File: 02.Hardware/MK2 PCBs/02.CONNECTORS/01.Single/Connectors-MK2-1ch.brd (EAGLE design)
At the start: 59.5 x 28.5 mm, 3 parts, among them K1 FLEX8

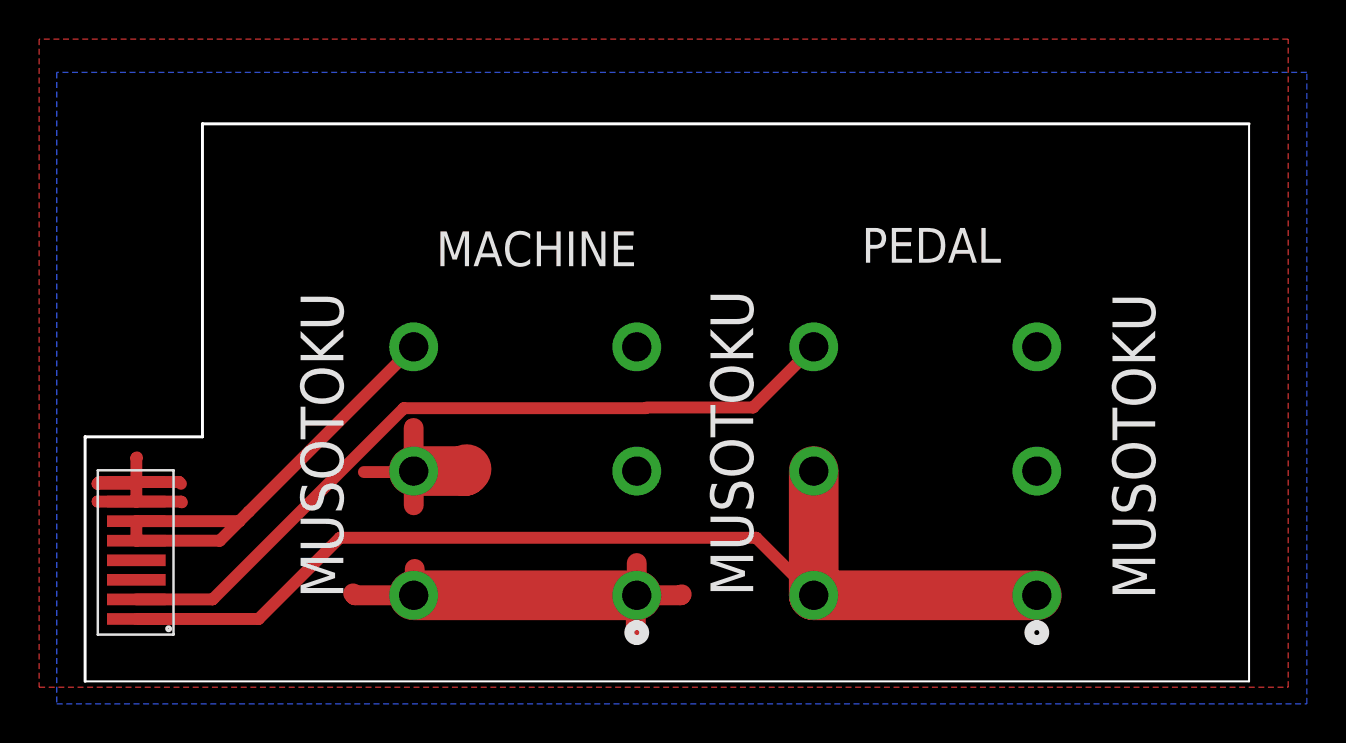
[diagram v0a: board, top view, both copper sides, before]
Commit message: Cambio Grosor y Carpetas nuevas
Se cambia el grosor de las pistas de VOUT y la conexión a las vías de los conectores.
----------
Creación de las carpetas dentro de la
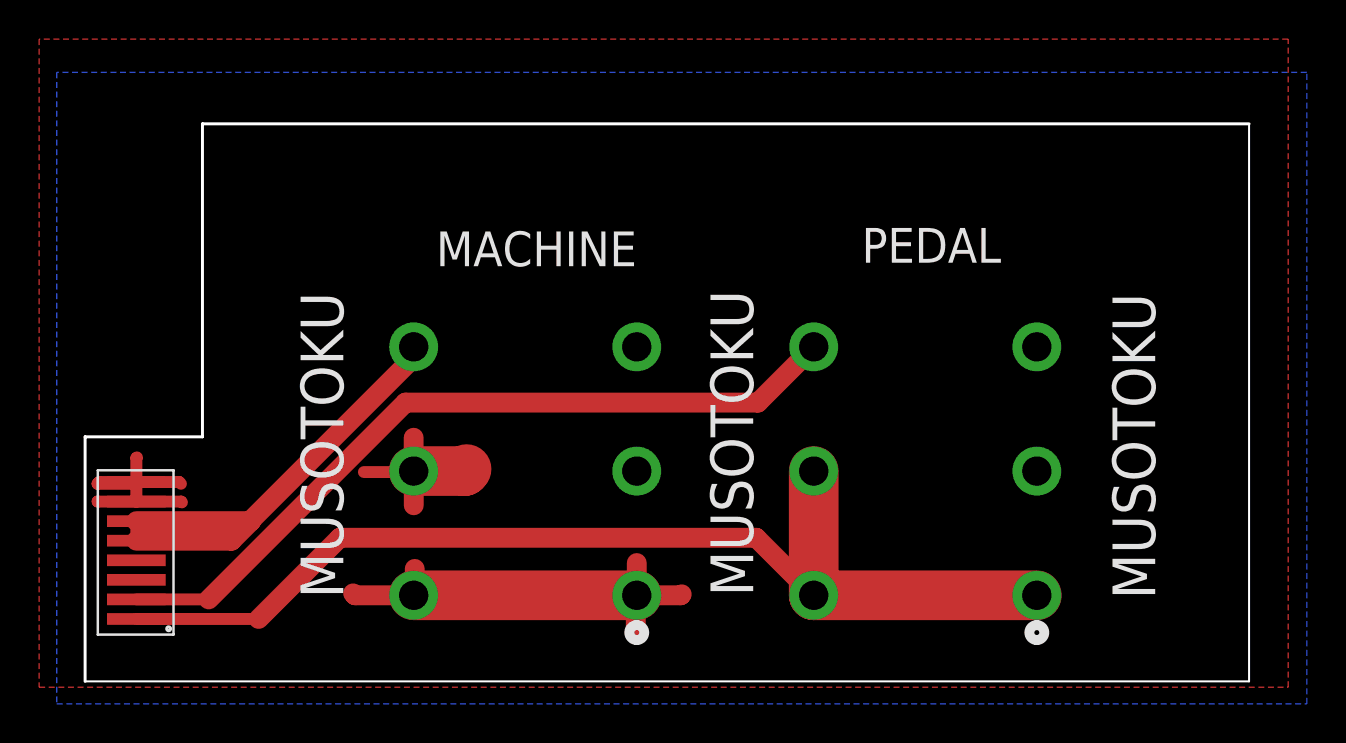
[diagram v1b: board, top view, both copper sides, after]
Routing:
- net VOUT: track 24.5 -> 25.5 mm
- net GND: track 50.9 -> 50.3 mm

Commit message: PCB 1channel - CAM output generado
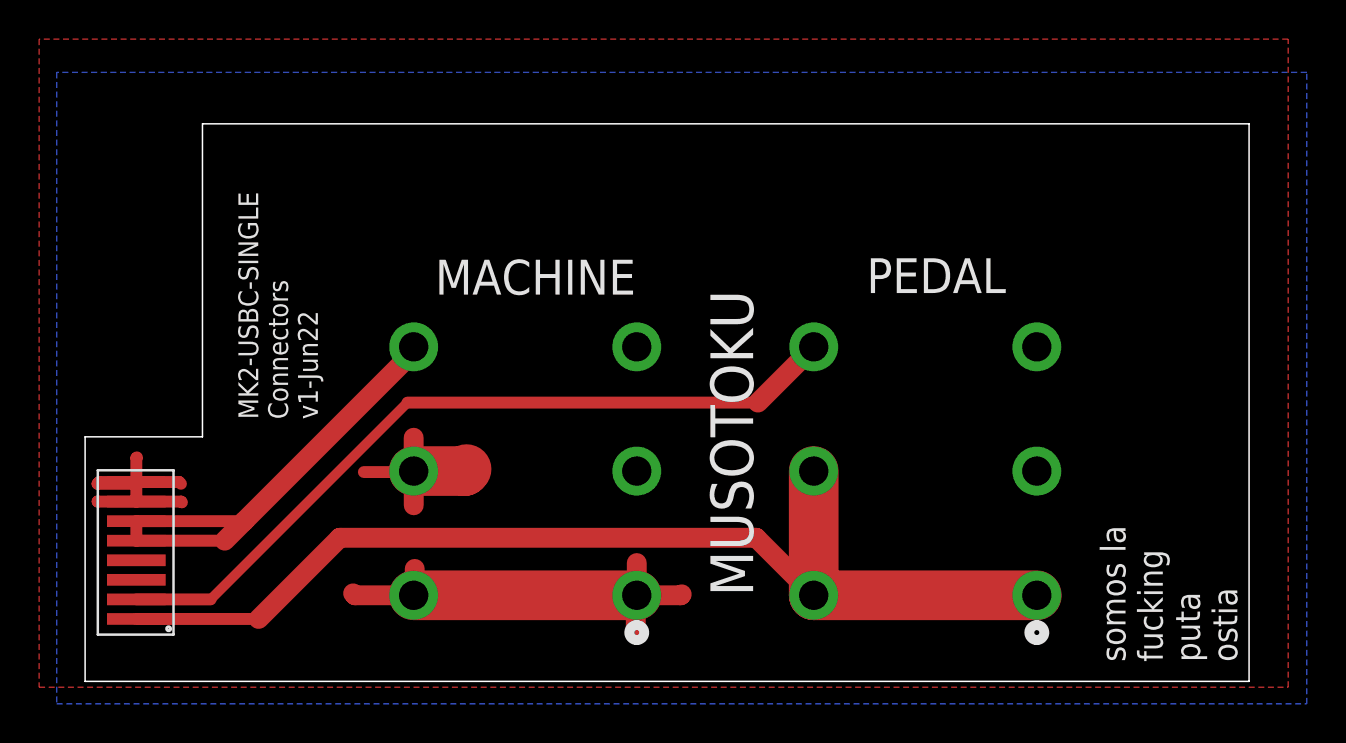
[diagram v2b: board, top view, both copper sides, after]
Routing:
- net VOUT: track 25.5 -> 24.9 mm
- added copper zone on layer 1, net VOUT
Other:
- board text added: "MK2-USBC-SINGLE Connectors v1-Jun22"
- board text removed: "MK2-USBC-SINGLE Connectors v1-May22"
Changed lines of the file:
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@@
 <drawing>
 <settings>
-<setting alwaysvectorfont="yes"/>
+<setting alwaysvectorfont="no"/>
 <setting verticaltext="up"/>
 </settings>
-<grid distance="0.05" unitdist="mm" unit="mm" style="lines" multiple="1" display="yes" altdistance="5" altunitdist="mil" altunit="mil"/>
+<grid distance="0.5" unitdist="mm" unit="mm" style="lines" multiple="1" display="yes" altdistance="5" altunitdist="mil" altunit="mil"/>
 <layers>
-<layer number="1" name="Top" color="4" fill="1" visible="yes" active="yes"/>
-<layer number="2" name="Route2" color="1" fill="3" visible="yes" active="yes"/>
-<layer number="15" name="Route15" color="4" fill="6" visible="yes" active="yes"/>
-<layer number="16" name="Bottom" color="1" fill="1" visible="yes" active="yes"/>
+<layer number="1" name="Top" color="4" fill="1" visible="no" active="yes"/>
+<layer number="2" name="Route2" color="1" fill="3" visible="no" active="yes"/>
+<layer number="15" name="Route15" color="4" fill="6" visible="no" active="yes"/>
+<layer number="16" name="Bottom" color="1" fill="1" visible="no" active="yes"/>
 <layer number="17" name="Pads" color="2" fill="1" visible="yes" active="yes"/>
 <layer number="18" name="Vias" color="2" fill="1" visible="yes" active="yes"/>
 <layer number="19" name="Unrouted" color="6" fill="1" visible="yes" active="yes"/>
 <layer number="20" name="Dimension" color="24" fill="1" visible="yes" active="yes"/>
-<layer number="21" name="tPlace" color="7" fill="1" visible="yes" active="yes"/>
+<layer number="21" name="tPlace" color="7" fill="1" visible="no" active="yes"/>
 <layer number="22" name="bPlace" color="7" fill="1" visible="yes" active="yes"/>
-<layer number="23" name="tOrigins" color="15" fill="1" visible="yes" active="yes"/>
+<layer number="23" name="tOrigins" color="15" fill="1" visible="no" active="yes"/>
 <layer number="24" name="bOrigins" color="15" fill="1" visible="yes" active="yes"/>
 <layer number="25" name="tNames" color="7" fill="1" visible="yes" active="yes"/>
@@
 <layer number="37" name="tTest" color="7" fill="1" visible="no" active="yes"/>
 <layer number="38" name="bTest" color="7" fill="1" visible="no" active="yes"/>
-<layer number="39" name="tKeepout" color="4" fill="11" visible="yes" active="yes"/>
+<layer number="39" name="tKeepout" color="4" fill="11" visible="no" active="yes"/>
 <layer number="40" name="bKeepout" color="1" fill="11" visible="yes" active="yes"/>
-<layer number="41" name="tRestrict" color="4" fill="10" visible="yes" active="yes"/>
+<layer number="41" name="tRestrict" color="4" fill="10" visible="no" active="yes"/>
 <layer number="42" name="bRestrict" color="1" fill="10" visible="yes" active="yes"/>
 <layer number="43" name="vRestrict" color="2" fill="10" visible="no" active="yes"/>
@@
 <layer number="46" name="Milling" color="3" fill="1" visible="no" active="yes"/>
 <layer number="47" name="Measures" color="7" fill="1" visible="no" active="yes"/>
-<layer number="48" name="Document" color="7" fill="1" visible="yes" active="yes"/>
+<layer number="48" name="Document" color="7" fill="1" visible="no" active="yes"/>
 <layer number="49" name="Reference" color="7" fill="1" visible="no" active="yes"/>
 <layer number="50" name="dxf" color="7" fill="1" visible="no" active="yes"/>
-<layer number="51" name="tDocu" color="7" fill="1" visible="yes" active="yes"/>
+<layer number="51" name="tDocu" color="7" fill="1" visible="no" active="yes"/>
 <layer number="52" name="bDocu" color="7" fill="1" visible="yes" active="yes"/>
 <layer number="53" name="tGND_GNDA" color="7" fill="9" visible="no" active="no"/>
@@
 <board>
 <plain>
-<text x="60.7" y="41.5" size="1.778" layer="25" font="vector" rot="R180">MACHINE </text>
-<text x="72.2" y="39.9" size="1.778" layer="25" font="vector">PEDAL</text>
-<text x="69.75" y="41.3" size="1.016" layer="26" font="vector" rot="MR0">MK2-USBC-SINGLE
+<text x="60.65" y="40.05" size="1.778" layer="25" font="vector" rot="R180">MACHINE </text>
+<text x="72.45" y="38.35" size="1.778" layer="25" font="vector">PEDAL</text>
+<text x="44.4" y="31.9" size="1.016" layer="25" font="vector" rot="R90">MK2-USBC-SINGLE
 Connectors
-v1-May22</text>
-<text x="78.3" y="23.75" size="1.016" layer="26" font="vector" rot="MR0">somos la
+v1-Jun22</text>
+<text x="91.4" y="19.5" size="1.27" layer="25" font="vector" rot="R90">somos la
 fucking
 puta
 ostia</text>
-<text x="45.7" y="22.75" size="2.1844" layer="25" font="vector" ratio="10" rot="R90">MUSOTOKU</text>
 <text x="66.65" y="22.85" size="2.1844" layer="25" font="vector" ratio="10" rot="R90">MUSOTOKU</text>
-<wire x1="32.5" y1="18.5" x2="92" y2="18.5" width="0.1016" layer="20"/>
-<wire x1="92" y1="18.5" x2="92" y2="47" width="0.1016" layer="20"/>
-<wire x1="32.5" y1="18.5" x2="32.5" y2="31" width="0.1524" layer="20"/>
-<wire x1="32.5" y1="31" x2="38.5" y2="31" width="0.1524" layer="20"/>
-<wire x1="38.5" y1="31" x2="38.5" y2="47" width="0.1524" layer="20"/>
-<wire x1="38.5" y1="47" x2="92" y2="47" width="0.1524" layer="20"/>
-<text x="87.2" y="22.7" size="2.1844" layer="25" font="vector" ratio="10" rot="R90">MUSOTOKU</text>
+<wire x1="32.5" y1="18.5" x2="92" y2="18.5" width="0.0762" layer="20"/>
+<wire x1="92" y1="18.5" x2="92" y2="47" width="0.0762" layer="20"/>
+<wire x1="32.5" y1="18.5" x2="32.5" y2="31" width="0.0762" layer="20"/>
+<wire x1="32.5" y1="31" x2="38.5" y2="31" width="0.0762" layer="20"/>
+<wire x1="38.5" y1="31" x2="38.5" y2="47" width="0.0762" layer="20"/>
+<wire x1="38.5" y1="47" x2="92" y2="47" width="0.0762" layer="20"/>
 <wire x1="56.2017" y1="34.50245" x2="56.2017" y2="33.08315" width="0.1" layer="48"/>
 <wire x1="71.2179" y1="13.08315" x2="111.2098" y2="13.08315" width="0.1" layer="48"/>
@@
 <circle x="69.7454" y="29.25" radius="0.75" width="0.1" layer="48"/>
 <circle x="69.7454" y="22.9" radius="0.75" width="0.1" layer="48"/>
+<polygon width="0.0762" layer="41">
+<vertex x="48.8" y="34.25"/>
+<vertex x="41.3" y="26.75"/>
+<vertex x="41.3" y="26.2"/>
+<vertex x="41.75" y="25.75"/>
+<vertex x="51.15" y="35.15"/>
+<vertex x="51.15" y="36.8"/>
+<vertex x="50.1" y="37.85"/>
+<vertex x="49.6" y="37.85"/>
+<vertex x="48.7" y="37.85"/>
+<vertex x="47.45" y="36.6"/>
+<vertex x="47.3" y="36.45"/>
+<vertex x="47.3" y="34.35"/>
+<vertex x="47.3" y="32.75"/>
+<vertex x="45.65" y="31.1"/>
+</polygon>
 </plain>
 <attributes>
@@
 <wire x1="35.12" y1="25.69" x2="35.12" y2="26.69" width="0.6096" layer="1"/>
 <contactref element="MACHINE3" pad="6"/>
-<wire x1="35.12" y1="26.69" x2="40.9354" y2="26.69" width="1.016" layer="1"/>
-<wire x1="40.9354" y1="26.69" x2="40.9854" y2="26.69" width="1.016" layer="1"/>
-<wire x1="40.9354" y1="26.69" x2="49.2954" y2="35.05" width="1.016" layer="1"/>
-<wire x1="49.2954" y1="35.05" x2="49.2954" y2="35.6" width="1.016" layer="1"/>
-<wire x1="35.12" y1="25.69" x2="39.9854" y2="25.69" width="1.016" layer="1"/>
-<wire x1="39.9854" y1="25.69" x2="40.9854" y2="26.69" width="1.016" layer="1"/>
+<wire x1="35.12" y1="26.69" x2="40.6354" y2="26.69" width="0.6096" layer="1"/>
+<wire x1="40.6354" y1="26.69" x2="49.2954" y2="35.35" width="1.016" layer="1"/>
+<wire x1="49.2954" y1="35.35" x2="49.2954" y2="35.6" width="1.016" layer="1"/>
+<wire x1="35.12" y1="25.69" x2="39.6354" y2="25.69" width="0.6096" layer="1"/>
+<wire x1="39.6354" y1="25.69" x2="40.6354" y2="26.69" width="1.016" layer="1"/>
+<polygon width="0.1524" layer="1">
+<vertex x="35.25" y="26.7"/>
+<vertex x="35.25" y="25.65"/>
+<vertex x="39.8" y="25.65"/>
+<vertex x="39.8" y="25.7"/>
+<vertex x="39.8" y="26.7"/>
+<vertex x="35.25" y="26.7"/>
+</polygon>
+<polygon width="0.1524" layer="1" thermals="no">
+<vertex x="35" y="26.5"/>
+<vertex x="35" y="25.5"/>
+<vertex x="40" y="25.5"/>
+<vertex x="40" y="26.5"/>
+</polygon>
 </signal>
 <signal name="SEL">
@@
 <contactref element="K1" pad="2"/>
 <contactref element="MACHINE4" pad="6"/>
-<wire x1="35.12" y1="22.69" x2="38.81868125" y2="22.69" width="0.6096" layer="1"/>
-<wire x1="48.87868125" y1="32.75" x2="66.8954" y2="32.75" width="1.016" layer="1"/>
+<wire x1="35.12" y1="22.69" x2="38.91868125" y2="22.69" width="0.6096" layer="1"/>
+<wire x1="48.97868125" y1="32.75" x2="66.8954" y2="32.75" width="0.6096" layer="1"/>
 <wire x1="66.8954" y1="32.75" x2="69.7454" y2="35.6" width="1.016" layer="1"/>
-<wire x1="38.81868125" y1="22.69" x2="48.87868125" y2="32.75" width="1.016" layer="1"/>
+<wire x1="38.91868125" y1="22.69" x2="48.97868125" y2="32.75" width="0.508" layer="1"/>
 </signal>
 </signals>
